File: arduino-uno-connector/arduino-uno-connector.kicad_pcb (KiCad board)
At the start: 2 copper layers, 121 x 69 mm, 13 parts, among them J1 Controller Connection, SW1 5V Switch, SW2 3V3 Switch, SW3 DIR_B / DIR_C, SW4 STP_B / STP_C

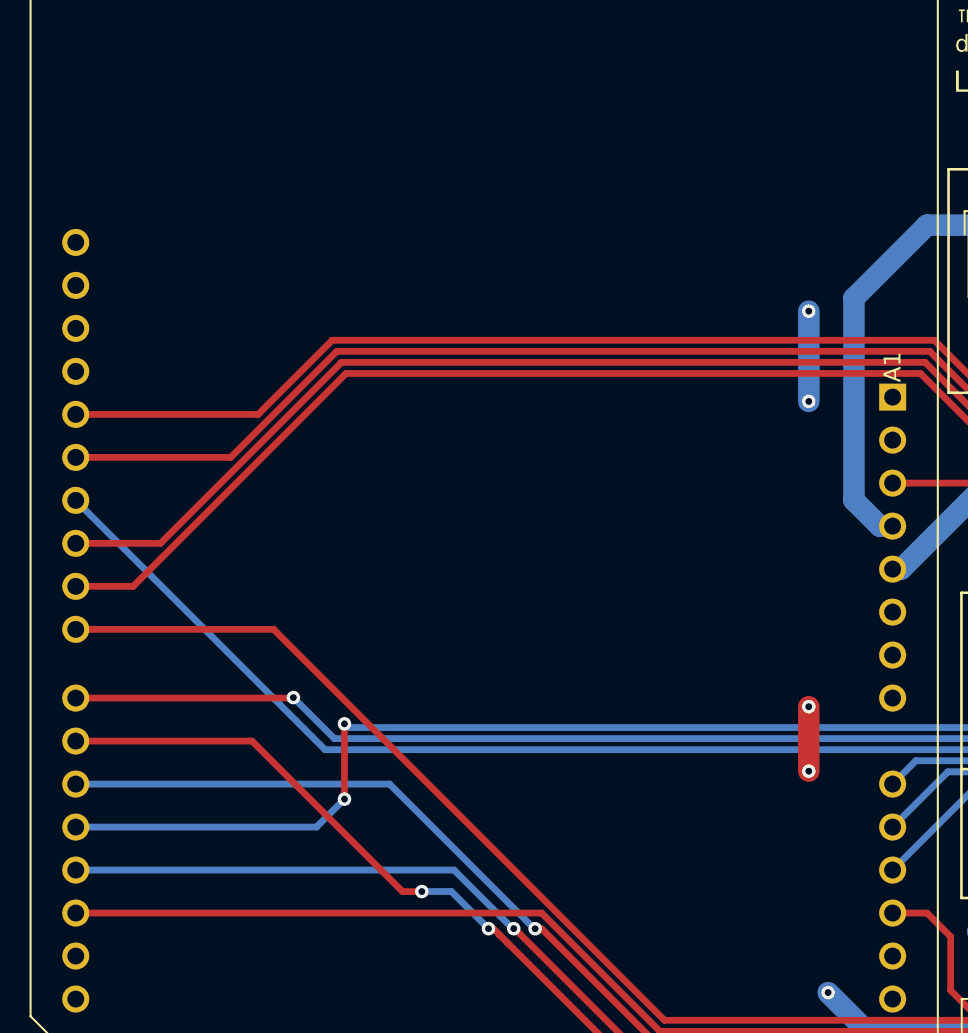
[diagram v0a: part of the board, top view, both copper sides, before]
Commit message: Updated Printing for Arduino and GRBL Reference
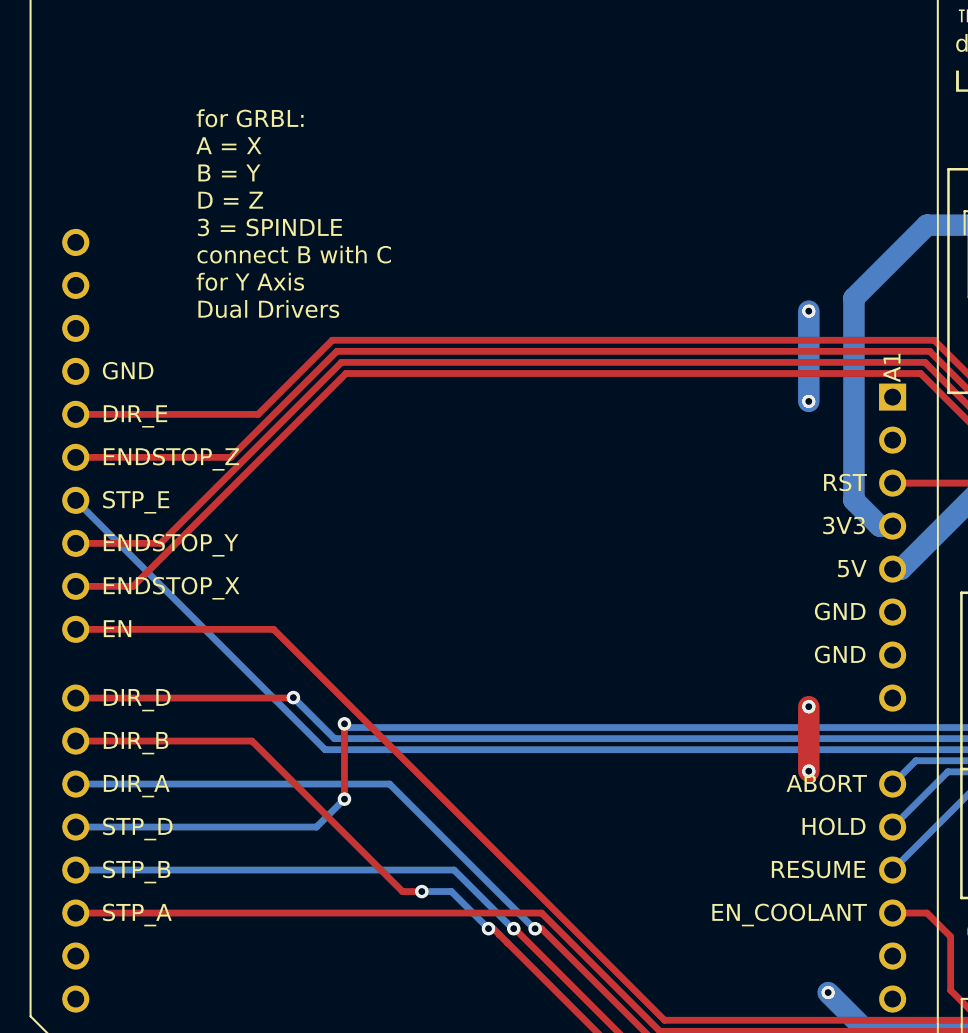
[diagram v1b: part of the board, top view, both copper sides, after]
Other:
- board text added: "ENDSTOP_X"
- board text added: "ENDSTOP_Y"
- board text added: "ENDSTOP_Z"
- board text added: "EN_COOLANT"
- board text added: "RST"
- board text added: "for GRBL: A = X B = Y D = Z 3 = SPINDLE connect B with C for Y Axis Dual Drivers"
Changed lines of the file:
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@@
   (gr_line (start 148 121) (end 148 116)
     (stroke (width 0.01) (type default)) (layer "User.1"))
+  (gr_text "GND" (at 44.704 82.804) (layer "F.SilkS" knockout)
+    (effects (font (size 1 1) (thickness 0.15)) (justify left))
+  )
   (gr_text "3V3" (at 102.489 106.807 90) (layer "F.SilkS")
     (effects (font (size 1 1) (thickness 0.15)) (justify right bottom))
   )
+  (gr_text "RESUME" (at 89.916 112.268) (layer "F.SilkS")
+    (effects (font (size 1 1) (thickness 0.15)) (justify right))
+  )
+  (gr_text "ENDSTOP_Y" (at 44.704 92.964) (layer "F.SilkS")
+    (effects (font (size 1 1) (thickness 0.15)) (justify left))
+  )
+  (gr_text "EN_COOLANT" (at 89.916 114.808) (layer "F.SilkS")
+    (effects (font (size 1 1) (thickness 0.15)) (justify right))
+  )
   (gr_text "V_EXT" (at 97.409 106.807 90) (layer "F.SilkS")
     (effects (font (size 1 1) (thickness 0.15)) (justify right bottom))
@@
   (gr_text "ENDSTOP_Y+" (at 126.619 105.791 90) (layer "F.SilkS")
     (effects (font (size 1 1) (thickness 0.15)) (justify left top))
+  )
+  (gr_text "HOLD" (at 89.916 109.728) (layer "F.SilkS")
+    (effects (font (size 1 1) (thickness 0.15)) (justify right))
   )
   (gr_text "LibreCNC ARDUINO CONNECTOR V1.0.1\n" (at 95.018 66.44) (layer "F.SilkS")
     (effects (font (size 1.25 1.25) (thickness 0.2)) (justify left bottom))
   )
+  (gr_text "GND" (at 89.916 97.028) (layer "F.SilkS" knockout)
+    (effects (font (size 1 1) (thickness 0.15)) (justify right))
+  )
+  (gr_text "DIR_B" (at 44.704 104.648) (layer "F.SilkS")
+    (effects (font (size 1 1) (thickness 0.15)) (justify left))
+  )
   (gr_text "EN_COOL" (at 105.029 106.807 90) (layer "F.SilkS")
     (effects (font (size 1 1) (thickness 0.15)) (justify right bottom))
@@
   (gr_text "DIR_A" (at 112.649 106.807 90) (layer "F.SilkS")
     (effects (font (size 1 1) (thickness 0.15)) (justify right bottom))
+  )
+  (gr_text "DIR_E" (at 44.704 85.344) (layer "F.SilkS")
+    (effects (font (size 1 1) (thickness 0.15)) (justify left))
   )
   (gr_text "connect Arduino 5V and \n3V3 with Periphery" (at 107.95 80.772) (layer "F.SilkS")
@@
     (effects (font (size 1 1) (thickness 0.15)) (justify left top))
   )
+  (gr_text "STP_A" (at 44.704 114.808) (layer "F.SilkS")
+    (effects (font (size 1 1) (thickness 0.15)) (justify left))
+  )
+  (gr_text "GND" (at 89.916 99.568) (layer "F.SilkS" knockout)
+    (effects (font (size 1 1) (thickness 0.15)) (justify right))
+  )
+  (gr_text "3V3" (at 89.916 91.948) (layer "F.SilkS")
+    (effects (font (size 1 1) (thickness 0.15)) (justify right))
+  )
   (gr_text "RESET" (at 108.839 105.918 90) (layer "F.SilkS")
     (effects (font (size 1 1) (thickness 0.15)) (justify left top))
@@
     (effects (font (size 1 1) (thickness 0.15)) (justify left top))
   )
+  (gr_text "STP_E" (at 44.704 90.424) (layer "F.SilkS")
+    (effects (font (size 1 1) (thickness 0.15)) (justify left))
+  )
   (gr_text "ENDSTOP_X-" (at 118.999 105.791 90) (layer "F.SilkS")
     (effects (font (size 1 1) (thickness 0.15)) (justify left top))
@@
     (effects (font (size 1 1) (thickness 0.15)) (justify left top))
   )
+  (gr_text "STP_B" (at 44.704 112.268) (layer "F.SilkS")
+    (effects (font (size 1 1) (thickness 0.15)) (justify left))
+  )
   (gr_text "5V" (at 99.949 106.807 90) (layer "F.SilkS")
     (effects (font (size 1 1) (thickness 0.15)) (justify right bottom))
+  )
+  (gr_text "ENDSTOP_X" (at 44.704 95.504) (layer "F.SilkS")
+    (effects (font (size 1 1) (thickness 0.15)) (justify left))
   )
   (gr_text "designed by Lukas Czycholl" (at 95.118 64.04) (layer "F.SilkS")
@@
     (effects (font (size 1 1) (thickness 0.2) bold) (justify bottom))
   )
+  (gr_text "ENDSTOP_Z" (at 44.704 87.884) (layer "F.SilkS")
+    (effects (font (size 1 1) (thickness 0.15)) (justify left))
+  )
   (gr_text "POWER CONNECTOR" (at 107.95 72.644) (layer "F.SilkS")
     (effects (font (size 1 1) (thickness 0.2) bold) (justify bottom))
   )
+  (gr_text "for GRBL:\nA = X\nB = Y\nD = Z\n3 = SPINDLE\nconnect B with C \nfor Y Axis \nDual Drivers\n" (at 50.292 79.756) (layer "F.SilkS")
+    (effects (font (size 1 1) (thickness 0.15)) (justify left bottom))
+  )
+  (gr_text "RST" (at 89.916 89.408) (layer "F.SilkS")
+    (effects (font (size 1 1) (thickness 0.15)) (justify right))
+  )
+  (gr_text "STP_D" (at 44.704 109.728) (layer "F.SilkS")
+    (effects (font (size 1 1) (thickness 0.15)) (justify left))
+  )
   (gr_text "ENDSTOP_Y-" (at 124.079 105.791 90) (layer "F.SilkS")
     (effects (font (size 1 1) (thickness 0.15)) (justify left top))
   )
+  (gr_text "DIR_A" (at 44.704 107.188) (layer "F.SilkS")
+    (effects (font (size 1 1) (thickness 0.15)) (justify left))
+  )
   (gr_text "STP_B" (at 115.189 106.807 90) (layer "F.SilkS")
     (effects (font (size 1 1) (thickness 0.15)) (justify right bottom))
@@
     (effects (font (size 1 1) (thickness 0.15)) (justify left top))
   )
+  (gr_text "DIR_D" (at 44.704 102.108) (layer "F.SilkS")
+    (effects (font (size 1 1) (thickness 0.15)) (justify left))
+  )
   (gr_text "EN" (at 107.569 106.807 90) (layer "F.SilkS")
     (effects (font (size 1 1) (thickness 0.15)) (justify right bottom))
   )
+  (gr_text "ABORT" (at 89.916 107.188) (layer "F.SilkS")
+    (effects (font (size 1 1) (thickness 0.15)) (justify right))
+  )
   (gr_text "STP_E" (at 130.429 106.807 90) (layer "F.SilkS")
     (effects (font (size 1 1) (thickness 0.15)) (justify right bottom))
+  )
+  (gr_text "EN" (at 44.704 98.044) (layer "F.SilkS")
+    (effects (font (size 1 1) (thickness 0.15)) (justify left))
   )
   (gr_text "ENDSTOP_Z-" (at 129.159 105.791 90) (layer "F.SilkS")
@@
   (gr_text "schematics and source:\ngithub.com/ITI-THM/LibreCNC" (at 121.318 63.94) (layer "F.SilkS")
     (effects (font (size 1 1) (thickness 0.15)) (justify left bottom))
+  )
+  (gr_text "5V" (at 89.916 94.488) (layer "F.SilkS")
+    (effects (font (size 1 1) (thickness 0.15)) (justify right))
   )
   (segment (start 108.331 99.095896) (end 98.643104 89.408) (width 0.4) (layer "F.Cu") (net 3))
@@
     (connect_pads (clearance 0.5))
     (min_thickness 0.25) (filled_areas_thickness no)
-    (fill yes (thermal_gap 0.5) (thermal_bridge_width 0.5))
+    (fill (thermal_gap 0.5) (thermal_bridge_width 0.5))
     (polygon
       (pts
@@
     (connect_pads (clearance 0.5))
     (min_thickness 0.25) (filled_areas_thickness no)
-    (fill yes (thermal_gap 0.5) (thermal_bridge_width 0.5))
+    (fill (thermal_gap 0.5) (thermal_bridge_width 0.5))
     (polygon
       (pts
